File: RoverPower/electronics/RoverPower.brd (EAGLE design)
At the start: 24.4 x 31.4 mm, 19 parts, among them IC1 INA168, IC3 TINY85, J1 I2C/ISP, U2 L7805

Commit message: Revised traces between bat/esc, added stop mask for tinning. Shrank board size significantly. Added labeling.
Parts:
- IC1: value INA168 -> INA139
- R1: device bt:R3921 -> bt:R2512
- moved R1 1.40 mm to (12.1, 13.2)
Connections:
- removed net BAT_V: BAT+.P$1, C1.1, IC1.3, R1.P$1, U2.1
- removed net ESC_V: ESC+.P$1, IC1.4, R1.P$2
- removed net V+: IC1.5, R3.2
- new net BAT+: BAT+.P$1, IC1.3, IC1.5, R1.P$1, R3.2
- new net ESC+: C1.1, ESC+.P$1, IC1.4, R1.P$2, U2.1
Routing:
- net BAT_V: track 31.6 -> 0.00 mm
- net ESC+: track 0.00 -> 21.5 mm
- net BAT+: track 0.00 -> 18.4 mm
- net ESC_V: track 9.42 -> 0.00 mm
- net V+: track 2.93 -> 0.00 mm
- added copper zone on layer 1, net BAT+
- added copper zone on layer 1, net ESC+
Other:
- board text added: "INA139"
- board text removed: "INA168"

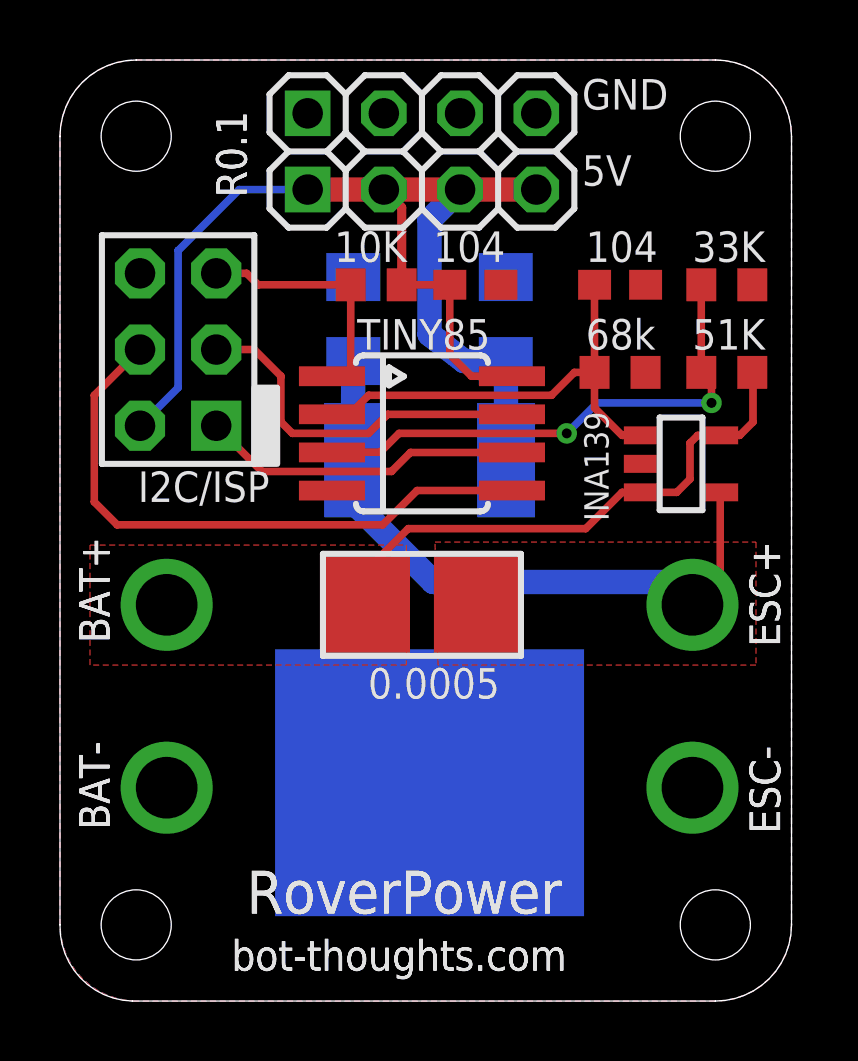
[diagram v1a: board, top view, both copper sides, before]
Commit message: Updated BAT+/ESC+ stop mask
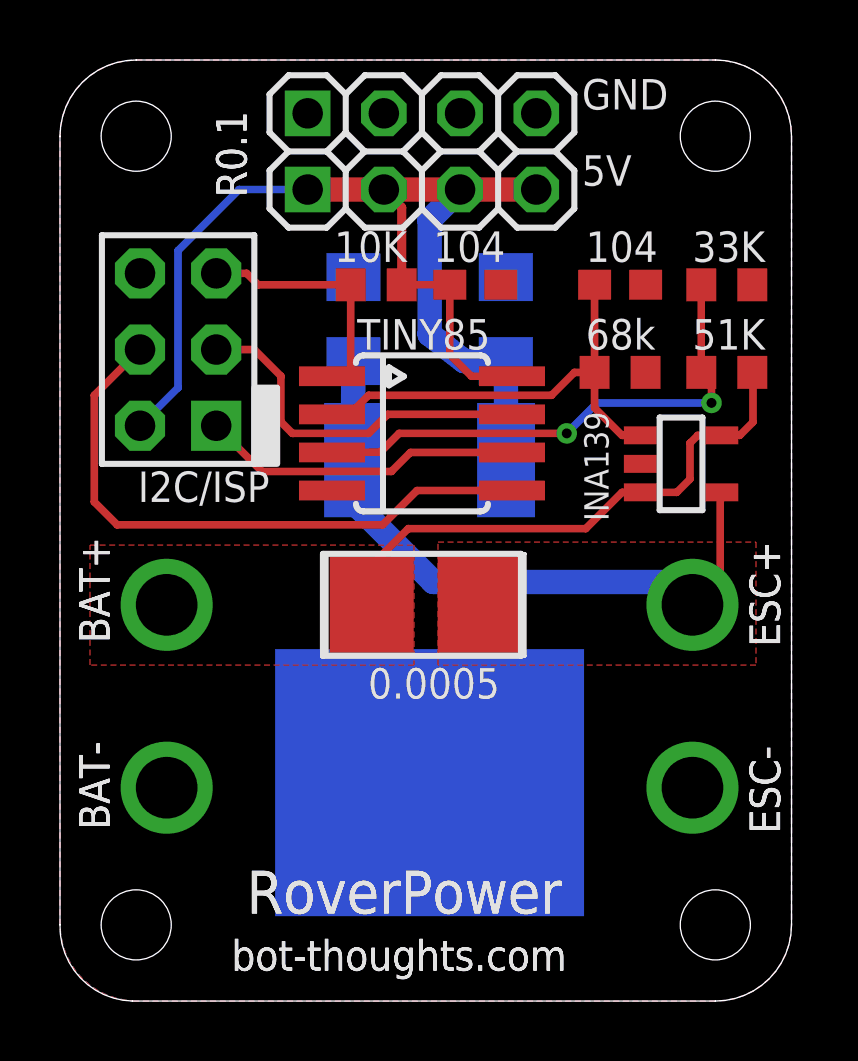
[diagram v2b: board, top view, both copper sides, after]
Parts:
- moved R1 0.13 mm to (12.2, 13.2)
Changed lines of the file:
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@@
 <layer number="19" name="Unrouted" color="6" fill="1" visible="yes" active="yes"/>
 <layer number="20" name="Dimension" color="15" fill="1" visible="yes" active="yes"/>
-<layer number="21" name="tPlace" color="7" fill="1" visible="no" active="yes"/>
-<layer number="22" name="bPlace" color="7" fill="1" visible="no" active="yes"/>
-<layer number="23" name="tOrigins" color="15" fill="1" visible="no" active="yes"/>
-<layer number="24" name="bOrigins" color="15" fill="1" visible="no" active="yes"/>
-<layer number="25" name="tNames" color="7" fill="1" visible="no" active="yes"/>
-<layer number="26" name="bNames" color="7" fill="1" visible="no" active="yes"/>
-<layer number="27" name="tValues" color="7" fill="1" visible="no" active="yes"/>
-<layer number="28" name="bValues" color="7" fill="1" visible="no" active="yes"/>
+<layer number="21" name="tPlace" color="7" fill="1" visible="yes" active="yes"/>
+<layer number="22" name="bPlace" color="7" fill="1" visible="yes" active="yes"/>
+<layer number="23" name="tOrigins" color="15" fill="1" visible="yes" active="yes"/>
+<layer number="24" name="bOrigins" color="15" fill="1" visible="yes" active="yes"/>
+<layer number="25" name="tNames" color="7" fill="1" visible="yes" active="yes"/>
+<layer number="26" name="bNames" color="7" fill="1" visible="yes" active="yes"/>
+<layer number="27" name="tValues" color="7" fill="1" visible="yes" active="yes"/>
+<layer number="28" name="bValues" color="7" fill="1" visible="yes" active="yes"/>
 <layer number="29" name="tStop" color="7" fill="3" visible="yes" active="yes"/>
 <layer number="30" name="bStop" color="7" fill="6" visible="yes" active="yes"/>
@@
 <polygon width="0.254" layer="29">
 <vertex x="3.694" y="15.3"/>
-<vertex x="21.014" y="15.3"/>
-<vertex x="21.014" y="11.2"/>
+<vertex x="11.616" y="15.3"/>
+<vertex x="11.616" y="11.2"/>
 <vertex x="3.694" y="11.2"/>
 </polygon>
@@
 <text x="16.256" y="21.463" size="1.016" layer="122" font="vector" ratio="20" rot="MR90">106</text>
 <text x="17.86049375" y="9.2075" size="1.27" layer="122" font="vector" ratio="16" rot="MR90">L7805</text>
+<polygon width="0.254" layer="29">
+<vertex x="12.838" y="15.3"/>
+<vertex x="21.014" y="15.3"/>
+<vertex x="21.014" y="11.2"/>
+<vertex x="12.838" y="11.2"/>
+</polygon>
 </plain>
 <attributes>
@@
 <attribute name="NAME" x="24.003" y="5.588" size="1.016" layer="25" font="vector" ratio="10" rot="R90"/>
 </element>
-<element name="R1" library="bt" package="R2512" value="0.0005" x="12.065" y="13.208" smashed="yes">
-<attribute name="VALUE" x="14.659" y="11.098" size="1.016" layer="27" font="vector" rot="R180"/>
+<element name="R1" library="bt" package="R2512" value="0.0005" x="12.192" y="13.208" smashed="yes">
+<attribute name="VALUE" x="14.786" y="11.098" size="1.016" layer="27" font="vector" rot="R180"/>
 </element>
 <element name="IC1" library="burr-brown" package="SOT23-5" value="INA139" x="20.701" y="17.907" smashed="yes" rot="R270">
@@
 <wire x1="17.526" y1="15.748" x2="11.608" y2="15.748" width="0.254" layer="1"/>
 <wire x1="11.608" y1="15.748" x2="10.271" y2="14.411" width="0.254" layer="1"/>
-<wire x1="10.265" y1="13.208" x2="10.271" y2="14.411" width="0.254" layer="1"/>
+<wire x1="10.392" y1="13.208" x2="10.271" y2="14.411" width="0.254" layer="1"/>
 <contactref element="BAT+" pad="P$1"/>
 <contactref element="R3" pad="2"/>
@@
 <polygon width="0.254" layer="1">
 <vertex x="1" y="15.2"/>
-<vertex x="11.546" y="15.2"/>
-<vertex x="11.546" y="11.2"/>
+<vertex x="11.8" y="15.2"/>
+<vertex x="11.8" y="11.2"/>
 <vertex x="1" y="11.2"/>
 </polygon>
@@
 <wire x1="20.32" y1="13.97" x2="21.082" y2="13.208" width="0.8128" layer="16"/>
 <polygon width="0.254" layer="1">
-<vertex x="12.5" y="15.3"/>
+<vertex x="12.6" y="15.3"/>
 <vertex x="23.2" y="15.3"/>
 <vertex x="23.2" y="11.2"/>

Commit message: Fixed Tiny label
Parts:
- IC3: value TINY85 -> TINY25
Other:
- board text added: "TINY25"
- board text removed: "TINY85"
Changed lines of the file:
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@@
 <layer number="19" name="Unrouted" color="6" fill="1" visible="yes" active="yes"/>
 <layer number="20" name="Dimension" color="15" fill="1" visible="yes" active="yes"/>
-<layer number="21" name="tPlace" color="7" fill="1" visible="yes" active="yes"/>
-<layer number="22" name="bPlace" color="7" fill="1" visible="yes" active="yes"/>
-<layer number="23" name="tOrigins" color="15" fill="1" visible="yes" active="yes"/>
-<layer number="24" name="bOrigins" color="15" fill="1" visible="yes" active="yes"/>
-<layer number="25" name="tNames" color="7" fill="1" visible="yes" active="yes"/>
-<layer number="26" name="bNames" color="7" fill="1" visible="yes" active="yes"/>
-<layer number="27" name="tValues" color="7" fill="1" visible="yes" active="yes"/>
-<layer number="28" name="bValues" color="7" fill="1" visible="yes" active="yes"/>
+<layer number="21" name="tPlace" color="7" fill="1" visible="no" active="yes"/>
+<layer number="22" name="bPlace" color="7" fill="1" visible="no" active="yes"/>
+<layer number="23" name="tOrigins" color="15" fill="1" visible="no" active="yes"/>
+<layer number="24" name="bOrigins" color="15" fill="1" visible="no" active="yes"/>
+<layer number="25" name="tNames" color="7" fill="1" visible="no" active="yes"/>
+<layer number="26" name="bNames" color="7" fill="1" visible="no" active="yes"/>
+<layer number="27" name="tValues" color="7" fill="1" visible="no" active="yes"/>
+<layer number="28" name="bValues" color="7" fill="1" visible="no" active="yes"/>
 <layer number="29" name="tStop" color="7" fill="3" visible="yes" active="yes"/>
 <layer number="30" name="bStop" color="7" fill="6" visible="yes" active="yes"/>
@@
 <vertex x="3.44" y="5"/>
 </polygon>
+<polygon width="0.254" layer="29">
+<vertex x="12.838" y="15.3"/>
+<vertex x="21.014" y="15.3"/>
+<vertex x="21.014" y="11.2"/>
+<vertex x="12.838" y="11.2"/>
+</polygon>
 <wire x1="21.414003125" y1="19.450990625" x2="21.414003125" y2="16.363009375" width="0.2032" layer="121"/>
 <wire x1="21.414003125" y1="16.363009375" x2="19.9890125" y2="16.363009375" width="0.2032" layer="121"/>
@@
 <wire x1="14.605" y1="28.956" x2="15.24" y2="28.321" width="0.2032" layer="121"/>
 <wire x1="16.51" y1="28.321" x2="15.24" y2="28.321" width="0.2032" layer="121"/>
-<wire x1="15.36499375" y1="14.907996875" x2="15.36499375" y2="11.508003125" width="0.2032" layer="121"/>
-<wire x1="8.76500625" y1="14.907996875" x2="8.76500625" y2="11.508003125" width="0.2032" layer="121"/>
-<wire x1="8.76500625" y1="14.907996875" x2="15.36499375" y2="14.907996875" width="0.2032" layer="121"/>
-<wire x1="15.36499375" y1="11.508003125" x2="8.76500625" y2="11.508003125" width="0.2032" layer="121"/>
+<wire x1="15.49199375" y1="14.907996875" x2="15.49199375" y2="11.508003125" width="0.2032" layer="121"/>
+<wire x1="8.89200625" y1="14.907996875" x2="8.89200625" y2="11.508003125" width="0.2032" layer="121"/>
+<wire x1="8.89200625" y1="14.907996875" x2="15.49199375" y2="14.907996875" width="0.2032" layer="121"/>
+<wire x1="15.49199375" y1="11.508003125" x2="8.89200625" y2="11.508003125" width="0.2032" layer="121"/>
 <text x="0.762" y="20.828" size="1.016" layer="122" font="vector" ratio="20" rot="MR90">sda</text>
 <text x="6.35" y="20.828" size="1.016" layer="122" font="vector" ratio="20" rot="MR90">scl</text>
@@
 <text x="12.446" y="24.638" size="1.016" layer="121" font="vector" ratio="20">104</text>
 <text x="18.288" y="16.002" size="0.8128" layer="121" font="vector" ratio="25" rot="R90">INA139</text>
-<text x="9.906" y="21.717" size="1.016" layer="121" font="vector" ratio="20">TINY85</text>
+<text x="9.906" y="21.717" size="1.016" layer="121" font="vector" ratio="20">TINY25</text>
 <text x="6.985" y="17.653" size="1.016" layer="121" font="vector" ratio="20" rot="R180">I2C/ISP</text>
 <text x="17.399" y="27.178" size="1.016" layer="121" font="vector" ratio="20">5V</text>
 <text x="17.399" y="29.718" size="1.016" layer="121" font="vector" ratio="20">GND</text>
-<text x="14.659" y="11.097996875" size="1.016" layer="121" font="vector" ratio="20" rot="R180">0.0005</text>
+<text x="14.786" y="11.097996875" size="1.016" layer="121" font="vector" ratio="20" rot="R180">0.0005</text>
 <text x="17.526" y="21.717" size="1.016" layer="121" font="vector" ratio="20">68k</text>
 <text x="21.082" y="21.717" size="1.016" layer="121" font="vector" ratio="20">51K</text>
@@
 <text x="16.256" y="21.463" size="1.016" layer="122" font="vector" ratio="20" rot="MR90">106</text>
 <text x="17.86049375" y="9.2075" size="1.27" layer="122" font="vector" ratio="16" rot="MR90">L7805</text>
-<polygon width="0.254" layer="29">
-<vertex x="12.838" y="15.3"/>
-<vertex x="21.014" y="15.3"/>
-<vertex x="21.014" y="11.2"/>
-<vertex x="12.838" y="11.2"/>
-</polygon>
 </plain>
 <attributes>
@@
 <attribute name="VALUE" x="6.985" y="17.653" size="1.016" layer="27" font="vector" ratio="16" rot="R180"/>
 </element>
-<element name="IC3" library="bt_avr" package="SOIC8" value="TINY85" x="12.065" y="18.923" smashed="yes" rot="R270">
+<element name="IC3" library="bt_avr" package="SOIC8" value="TINY25" x="12.065" y="18.923" smashed="yes" rot="R270">
 <attribute name="VALUE" x="9.906" y="21.717" size="1.016" layer="27" font="vector" ratio="10"/>
 </element>
